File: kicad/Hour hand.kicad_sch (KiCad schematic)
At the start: 64 parts, among them U001 74HC595, U002 74HC595

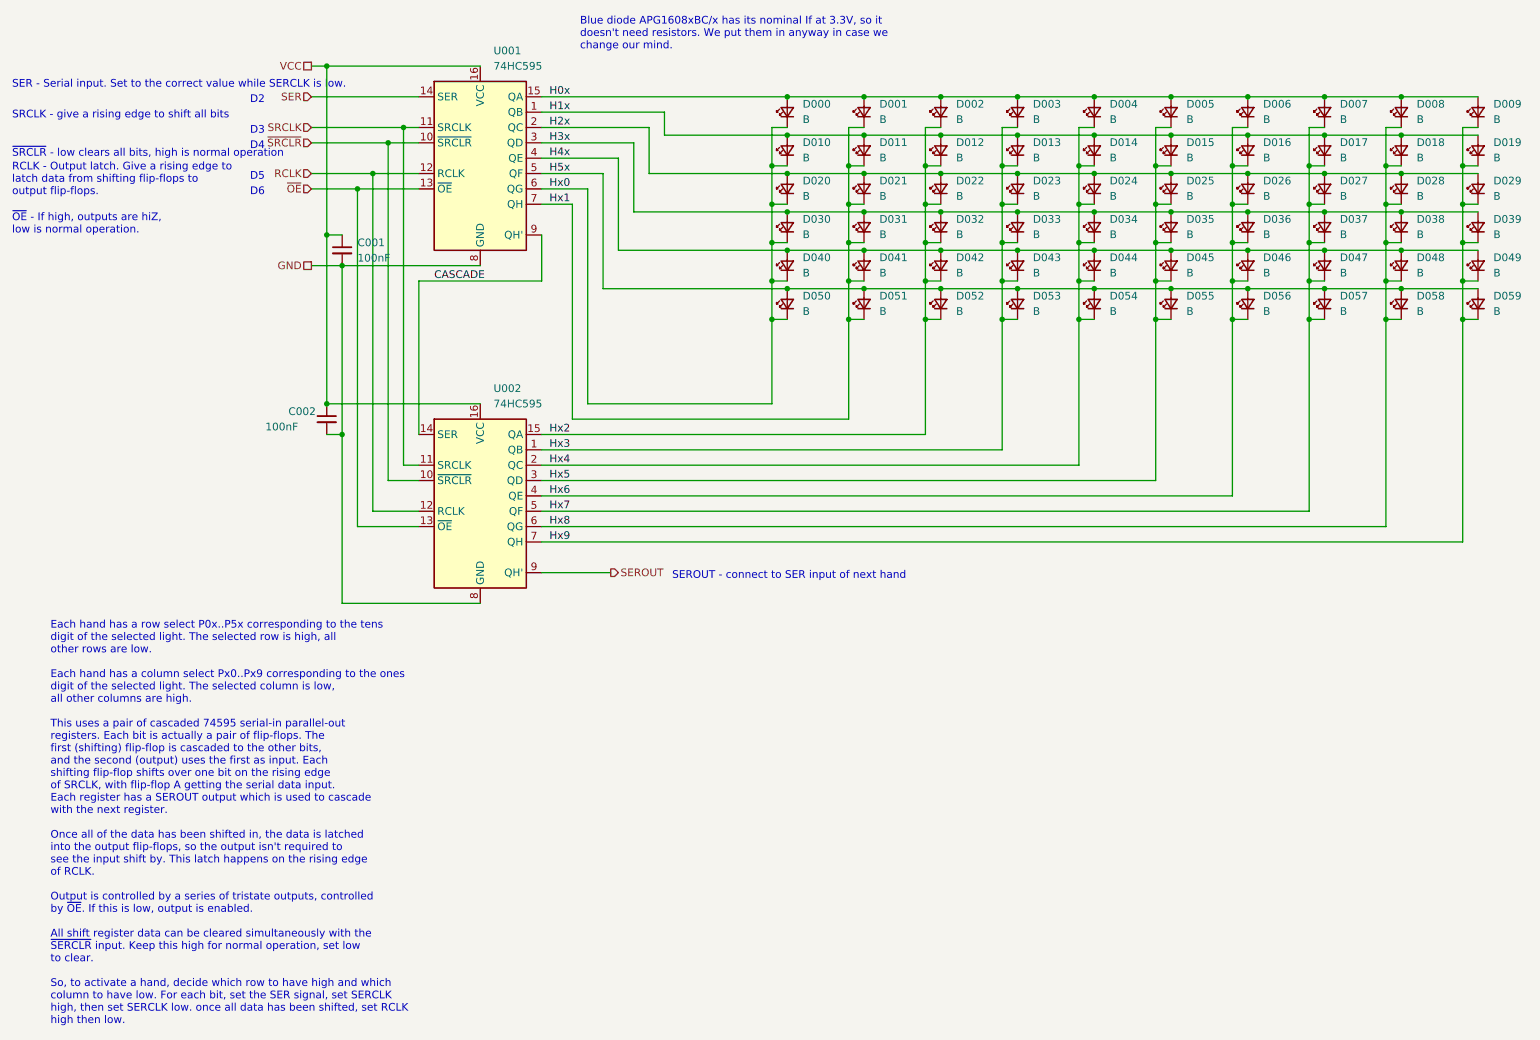
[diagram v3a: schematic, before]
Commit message: Continue wiring MOSFET switches
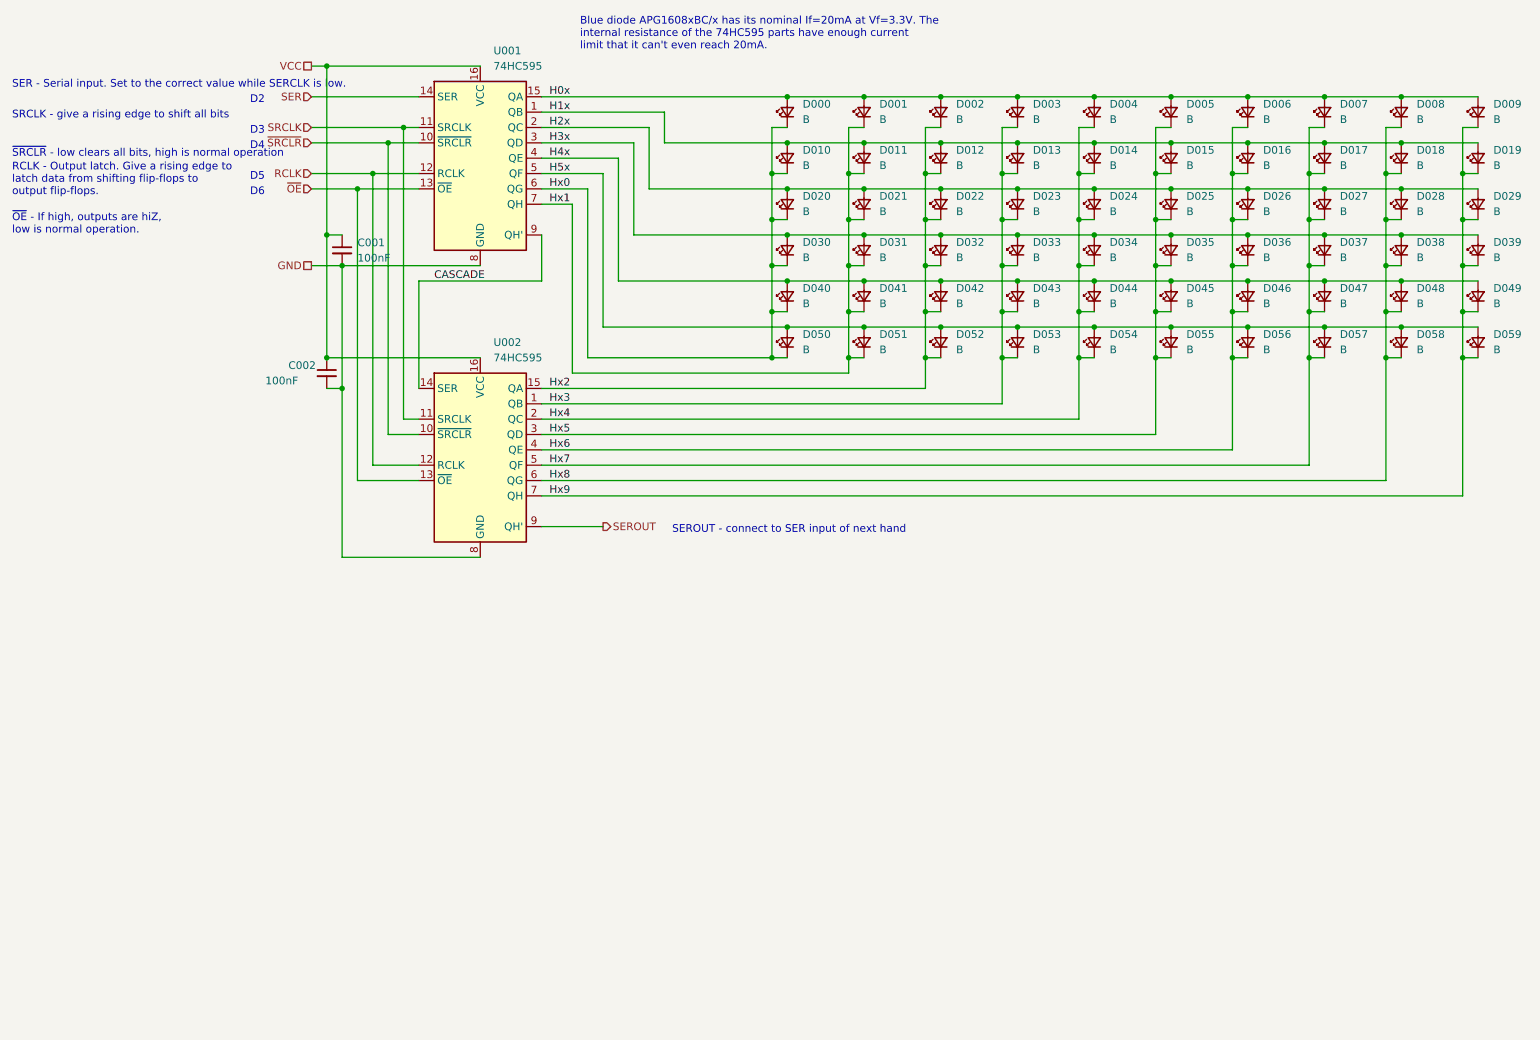
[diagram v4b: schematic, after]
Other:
- note added: "Blue diode APG1608xBC/x has its nominal If=20mA at Vf=3.3V. The internal resistance of the 74HC595 parts have enough current limit that it can't even reach 20mA."
- note removed: "Blue diode APG1608xBC/x has its nominal If at 3.3V, so it doesn't need resistors. We put them in anyway in case we change our mind."
- note removed: "Each hand has a row select P0x..P5x corresponding to the tens digit of the selected light. The selected row is high, all other rows are low. Each hand has a column select Px0..Px9 corresponding to the ones digit of the selected light. The selected column is low, all other columns are high. This uses a pair of cascaded 74595 serial-in parallel-out registers. Each bit is actually a pair of flip-flo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"
- moved on the sheet: C002, D010, D011, D012, D013, D014, D015, D016, D017, D018, D019, D020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

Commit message: Matrix8x8 stuff
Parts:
- removed C001, C002: 100nF, Capacitor_SMD:C_0603_1608Metric, symbol Device:C_Small
- removed D000, D001, D002, D003, D004, D005, D006, D007, D008, D009, D010, D011, D012, D013, D014, D015, D016, D017, D018, D019, D020, D021, D022, D023, D024, D025, D026, D027, D028, D029, D030, D031, D032, D033, D034, D035, D036, D037, D038, D039, D040, D041, D042, D043, D044, D045, D046, D047, D048, D049, D050, D051, D052, D053, D054, D055, D056, D057, D058, D059: B, LED_SMD:LED_0603_1608Metric, symbol Device:LED_Small
- removed U001, U002: 74HC595, Package_SO:TSSOP-16_4.4x5mm_P0.65mm, symbol 74xx:74HC595
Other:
- note removed: "Blue diode APG1608xBC/x has its nominal If=20mA at Vf=3.3V. The internal resistance of the 74HC595 parts have enough current limit that it can't even reach 20mA."
- note removed: "D2"
- note removed: "D3"
- note removed: "D4"
- note removed: "D5"
- note removed: "D6"
- note removed: "RCLK - Output latch. Give a rising edge to latch data from shifting flip-flops to output flip-flops."
- note removed: "SER - Serial input. Set to the correct value while SERCLK is low."
- note removed: "SEROUT - connect to SER input of next hand"
- note removed: "SRCLK - give a rising edge to shift all bits"
- note removed: "~{OE} - If high, outputs are hiZ, low is normal operation."
- note removed: "~{SRCLR} - low clears all bits, high is normal operation"
